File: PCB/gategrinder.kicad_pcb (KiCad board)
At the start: 2 copper layers, 177 x 96 mm, 71 parts, among them J1 EURO_PWR_2x5, J10 AudioJack3_SwitchTR, J3 Conn_01x14, J6 AudioJack3_SwitchTR, J7 AudioJack3_SwitchTR, J8 AudioJack3_SwitchTR, J9 AudioJack3_SwitchTR, Q1 BC547, Q2 BC547, Q3 BC547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

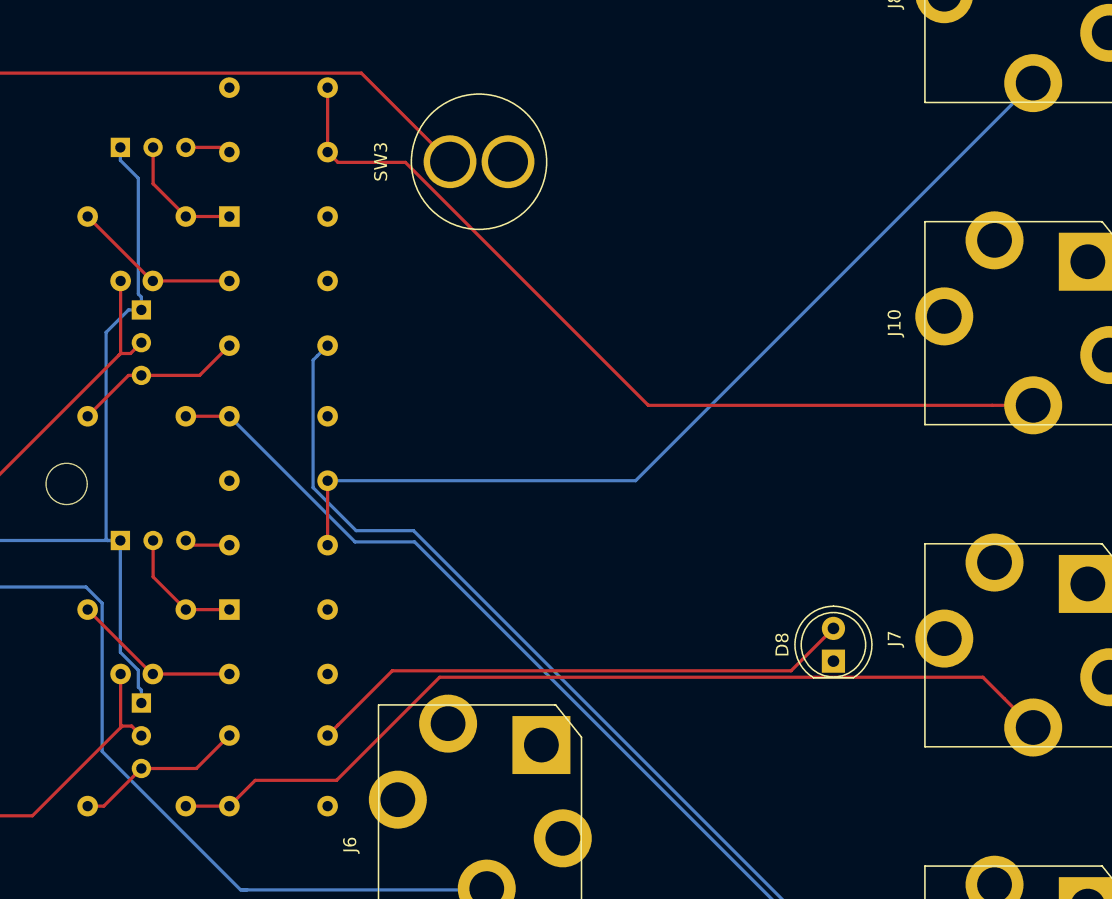
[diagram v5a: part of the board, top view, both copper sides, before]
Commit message: Replace fixed resistor output voltage dividers with trimmers
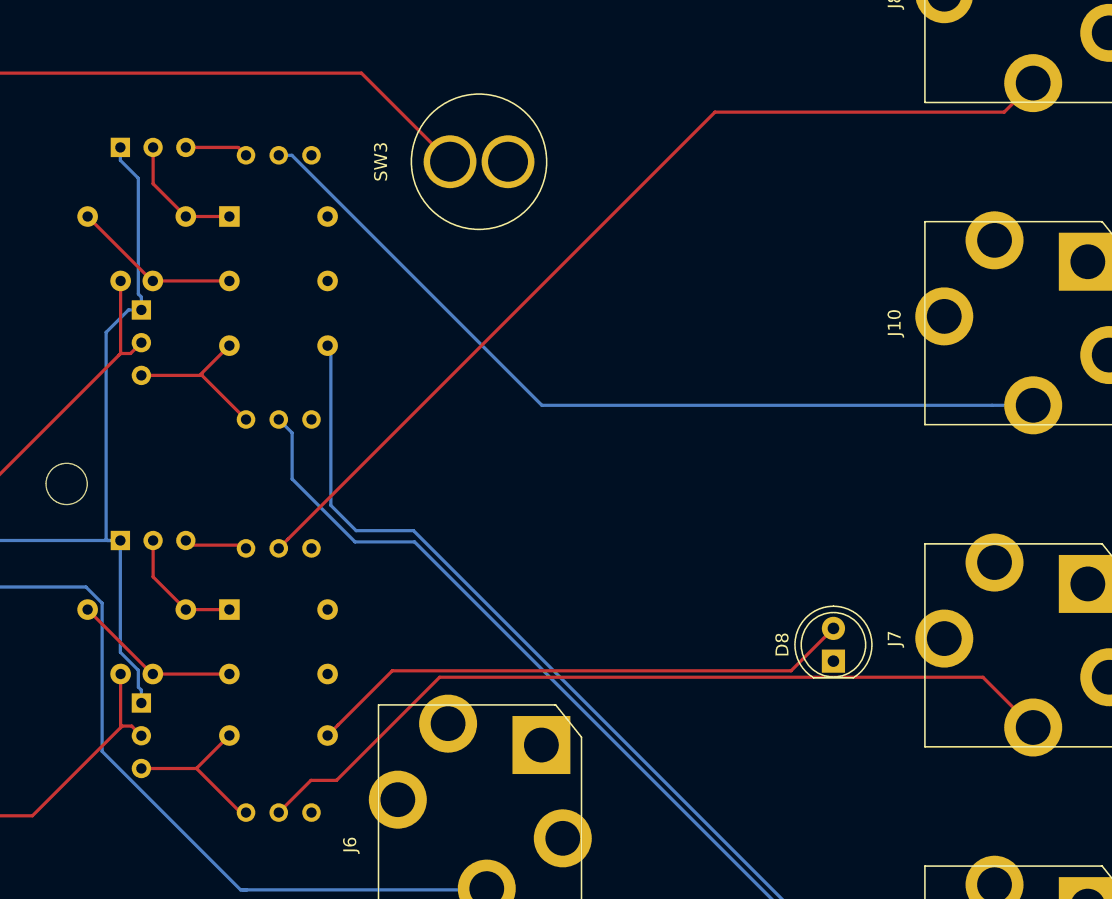
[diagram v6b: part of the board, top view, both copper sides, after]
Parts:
- removed R19, R21, R23, R25: 1k8, Resistor_THT:R_Axial_DIN0207_L6.3mm_D2.5mm_P7.62mm_Horizontal
- removed R20, R22, R24, R26: 1k, Resistor_THT:R_Axial_DIN0207_L6.3mm_D2.5mm_P7.62mm_Horizontal
- added RV1: 2k, Potentiometer_THT:Potentiometer_Bourns_3296W_Vertical, B.Cu at (154.0, 137.5)
- added RV2: 2k, Potentiometer_THT:Potentiometer_Bourns_3296W_Vertical, B.Cu at (154.0, 107.0)
- added RV3: 2k, Potentiometer_THT:Potentiometer_Bourns_3296W_Vertical, B.Cu at (154.0, 117.0)
- added RV4: 2k, Potentiometer_THT:Potentiometer_Bourns_3296W_Vertical, B.Cu at (154.0, 86.5)
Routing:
- net /GATE_INV_OUT: track 71.5 -> 64.5 mm
- net /GATE_OUT: track 88.8 -> 83.6 mm
- net Net-(Q4-Pad3): track 3.53 -> 4.92 mm
- net Net-(Q5-Pad3): track 3.53 -> 4.92 mm
- net /GATE_ON: track 67.9 -> 66.6 mm
- net /GATE_OFF: track 72.5 -> 73.5 mm
- net /GATE_LED: track 66.7 -> 65.8 mm
- net Net-(Q3-Pad3): track 13.3 -> 12.7 mm

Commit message: NA556 -> NE556N
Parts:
- U1: value NA556 -> NE556N
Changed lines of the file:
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@@
       (effects (font (size 1 1) (thickness 0.15)) (justify mirror))
     )
-    (fp_text value NA556 (at 3.81 -17.57 90) (layer B.Fab)
+    (fp_text value NE556N (at 3.81 -17.57 90) (layer B.Fab)
       (effects (font (size 1 1) (thickness 0.15)) (justify mirror))
     )

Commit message: Added pulldown for OR
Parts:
- added R19: 100k, Resistor_THT:R_Axial_DIN0207_L6.3mm_D2.5mm_P7.62mm_Horizontal, B.Cu at (51.0, 125.0)
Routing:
- net Net-(D3-Pad1): track 36.5 -> 41.5 mm
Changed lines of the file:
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@@
     (thickness 1.6)
     (drawings 14)
-    (tracks 308)
+    (tracks 309)
     (zones 0)
-    (modules 67)
+    (modules 68)
     (nets 68)
   )
@@
     (add_net VCC)
   )
+  (module Resistor_THT:R_Axial_DIN0207_L6.3mm_D2.5mm_P7.62mm_Horizontal (layer B.Cu)
+    (at 51 125 270)
+    (descr "Resistor, Axial_DIN0207 series, Axial, Horizontal, pin pitch=7.62mm, 0.25W = 1/4W, length*diameter=6.3*2.5mm^2, http://cdn-reichelt.de/documents/datenblatt/B400/1_4W%23YAG.pdf")
+    (tags "Resistor Axial_DIN0207 series Axial Horizontal pin pitch 7.62mm 0.25W = 1/4W length 6.3mm diameter 2.5mm")
+    (fp_text reference R19 (at 3.81 2.37 90) (layer B.SilkS)
+      (effects (font (size 1 1) (thickness 0.15)) (justify mirror))
+    )
+    (fp_text value 100k (at 3.81 -2.37 90) (layer B.Fab)
+      (effects (font (size 1 1) (thickness 0.15)) (justify mirror))
+    )
+    (fp_text user %R (at 3.81 0 90) (layer B.Fab)
+      (effects (font (size 1 1) (thickness 0.15)) (justify mirror))
+    )
+    (fp_line (start 8.67 1.5) (end -1.05 1.5) (layer B.CrtYd) (width 0.05))
+    (fp_line (start 8.67 -1.5) (end 8.67 1.5) (layer B.CrtYd) (width 0.05))
+    (fp_line (start -1.05 -1.5) (end 8.67 -1.5) (layer B.CrtYd) (width 0.05))
+    (fp_line (start -1.05 1.5) (end -1.05 -1.5) (layer B.CrtYd) (width 0.05))
+    (fp_line (start 7.08 -1.37) (end 7.08 -1.04) (layer B.SilkS) (width 0.12))
+    (fp_line (start 0.54 -1.37) (end 7.08 -1.37) (layer B.SilkS) (width 0.12))
+    (fp_line (start 0.54 -1.04) (end 0.54 -1.37) (layer B.SilkS) (width 0.12))
+    (fp_line (start 7.08 1.37) (end 7.08 1.04) (layer B.SilkS) (width 0.12))
+    (fp_line (start 0.54 1.37) (end 7.08 1.37) (layer B.SilkS) (width 0.12))
+    (fp_line (start 0.54 1.04) (end 0.54 1.37) (layer B.SilkS) (width 0.12))
+    (fp_line (start 7.62 0) (end 6.96 0) (layer B.Fab) (width 0.1))
+    (fp_line (start 0 0) (end 0.66 0) (layer B.Fab) (width 0.1))
+    (fp_line (start 6.96 1.25) (end 0.66 1.25) (layer B.Fab) (width 0.1))
+    (fp_line (start 6.96 -1.25) (end 6.96 1.25) (layer B.Fab) (width 0.1))
+    (fp_line (start 0.66 -1.25) (end 6.96 -1.25) (layer B.Fab) (width 0.1))
+    (fp_line (start 0.66 1.25) (end 0.66 -1.25) (layer B.Fab) (width 0.1))
+    (pad 2 thru_hole oval (at 7.62 0 270) (size 1.6 1.6) (drill 0.8) (layers *.Cu *.Mask)
+      (net 1 GND))
+    (pad 1 thru_hole circle (at 0 0 270) (size 1.6 1.6) (drill 0.8) (layers *.Cu *.Mask)
+      (net 20 "Net-(D3-Pad1)"))
+    (model ${KISYS3DMOD}/Resistor_THT.3dshapes/R_Axial_DIN0207_L6.3mm_D2.5mm_P7.62mm_Horizontal.wrl
+      (at (xyz 0 0 0))
+      (scale (xyz 1 1 1))
+      (rotate (xyz 0 0 0))
+    )
+  )
   (module Potentiometer_THT:Potentiometer_Bourns_3296W_Vertical (layer B.Cu)
     (at 154 86.5)
@@
   (segment (start 54.92206 125) (end 55.97206 125) (width 0.25) (layer F.Cu) (net 20))
   (segment (start 70.97206 140) (end 70.97206 141.45) (width 0.25) (layer F.Cu) (net 20))
+  (segment (start 51 125) (end 55.97206 125) (width 0.25) (layer F.Cu) (net 20))
   (segment (start 103.97206 127.25) (end 107.97206 127.25) (width 0.25) (layer F.Cu) (net 21) (status 30))
   (segment (start 113.05206 123.22) (end 113.05206 122.25) (width 0.25) (layer F.Cu) (net 21))
